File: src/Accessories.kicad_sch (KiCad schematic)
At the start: 20 parts

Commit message: Update Schematics design
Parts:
- removed D?: LED_Dual_Red_Green, LED_THT:LED_D5.0mm-3, symbol Device:LED_Dual_AAK
- removed R? (x2): 200R, Resistor_THT:R_Axial_DIN0204_L3.6mm_D1.6mm_P5.08mm_Horizontal, symbol Device:R
- added D? (x2): LED Yellow, LED_THT:LED_D5.0mm, symbol Device:LED
- added R? (x2): 470R, Resistor_THT:R_Axial_DIN0204_L3.6mm_D1.6mm_P5.08mm_Horizontal, symbol Device:R
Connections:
- net LowBat: now also R?.2
- net GND1 renamed GNDDash
- net GNDDash: now also D?.1 (K), D?.1 (K)
- net HighBat renamed PLight
- net PLight: now also R?.2
- new net: D?.2 (A), R?.1 (x2)
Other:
- note added: "Low battery indicator"
- note removed: "Battery indicator"
- moved on the sheet: D?, R?

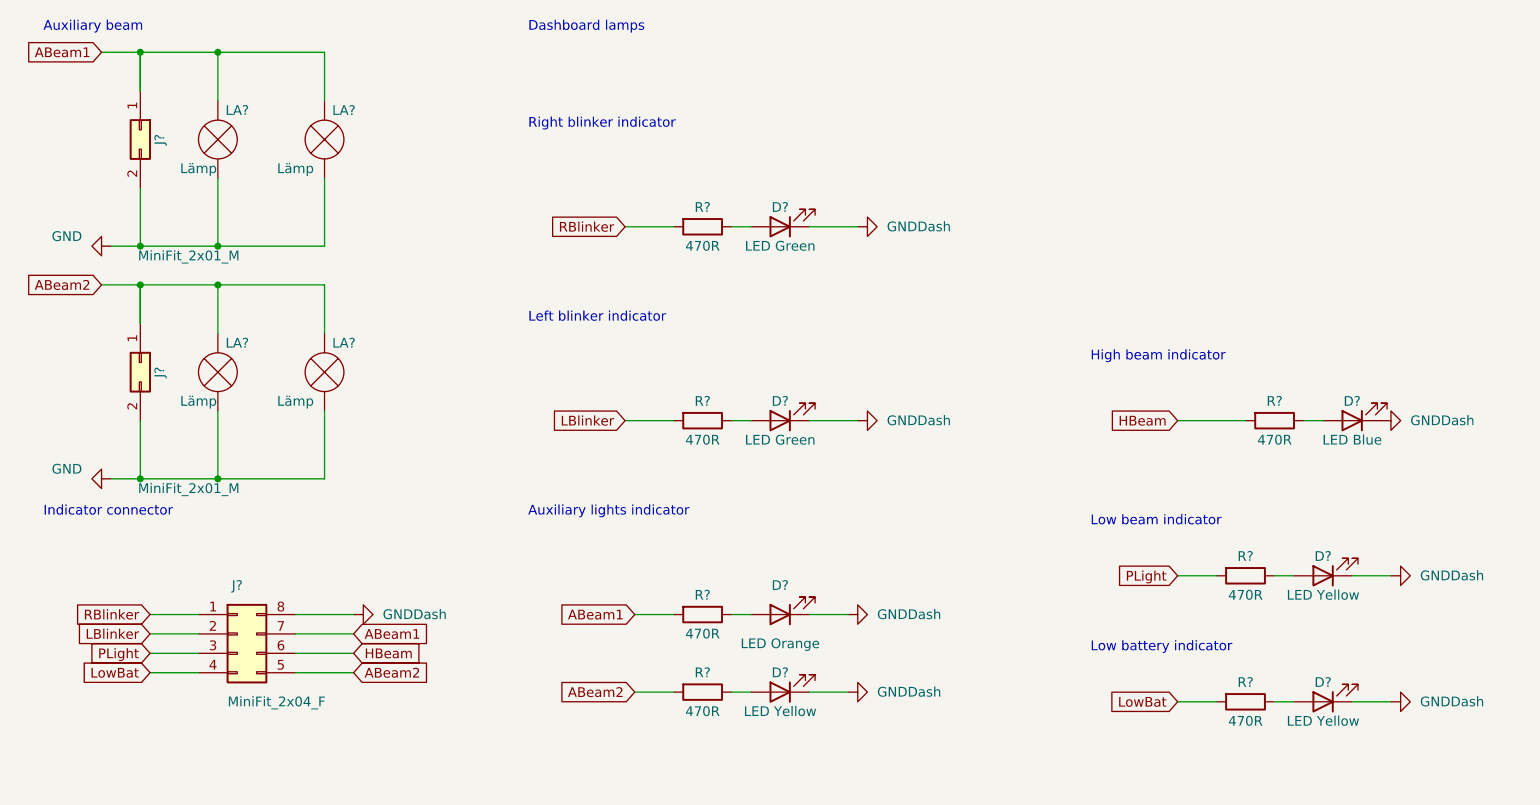
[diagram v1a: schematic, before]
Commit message: Add radio backup battery circuit; Update cable harness; rework main board circuit
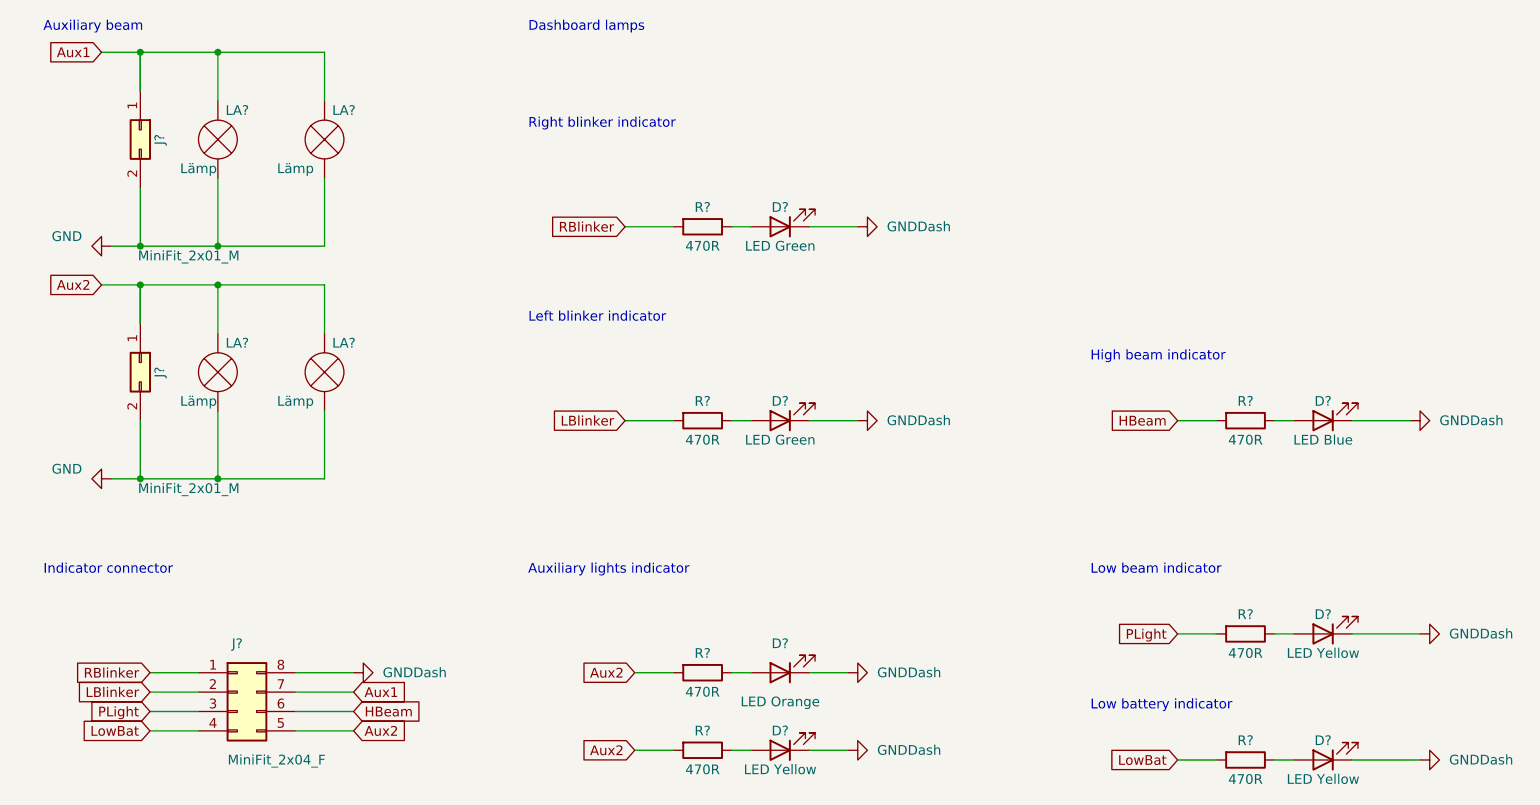
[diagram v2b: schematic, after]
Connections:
- net ABeam1 renamed Aux1
- net Aux1: no longer R?.2
- net ABeam2 renamed Aux2
- net Aux2: now also R?.2
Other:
- moved on the sheet: D?, J?, R?

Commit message: update Schematics
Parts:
- removed D? (x3): LED Yellow, LED_THT:LED_D5.0mm, symbol Device:LED
- removed J?: MiniFit_2x04_F, Connector_Molex:Molex_Mini-Fit_Jr_5566-08A_2x04_P4.20mm_Vertical, symbol Connector_Generic:Conn_02x04_Counter_Clockwise
- removed R? (x3): 470R, Resistor_THT:R_Axial_DIN0204_L3.6mm_D1.6mm_P5.08mm_Horizontal, symbol Device:R
- added D?: LED Green, LED_THT:LED_D5.0mm, symbol Device:LED
- added J?: MiniFit_2x03_F, Connector_Molex:Molex_Mini-Fit_Jr_5566-06A_2x03_P4.20mm_Vertical, symbol Connector_Generic:Conn_02x03_Counter_Clockwise
- added R?: 470R, Resistor_THT:R_Axial_DIN0204_L3.6mm_D1.6mm_P5.08mm_Horizontal, symbol Device:R
- D?: value LED Green -> LED Red
- D?: value LED Orange -> LED Yellow
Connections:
- net GNDDash: now also D?.1 (K), J?.6 (Pin_6)
- net HBeam: now also J?.5 (Pin_5)
- net LBlinker: now also J?.2 (Pin_2)
- net LowBat: now also R?.2, J?.3 (Pin_3)
- net RBlinker: now also J?.1 (Pin_1), R?.2; no longer R?.2
- net Aux1 renamed AuxHBeam
- net Aux2 renamed AuxLBeam
- net AuxLBeam: no longer R?.2
- new net: D?.2 (A), R?.1
- new net AuxBeams: J?.4 (Pin_4), R?.2
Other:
- note added: "Auxiliary beams"
- note added: "Auxiliary lights indicators"
- note added: "High beams"
- note added: "Indicators connector"
- note added: "Left signal indicator"
- note added: "Low battery Indicator"
- note added: "Medium beams"
- note added: "Right signal indicator"
- note removed: "Auxiliary beam"
- note removed: "Auxiliary lights indicator"
- note removed: "Indicator connector"
- note removed: "Left blinker indicator"
- note removed: "Low battery indicator"
- note removed: "Low beam indicator"
- note removed: "Right blinker indicator"
- moved on the sheet: D?, J?, LA?, R?

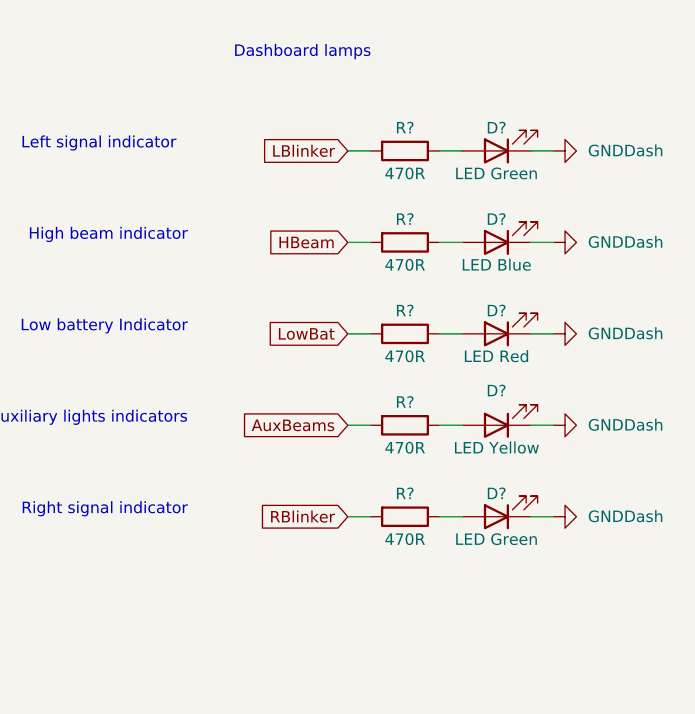
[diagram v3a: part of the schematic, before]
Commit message: Update Schmatics; Cleanup unecessary circuits; Simplify blinkers dimmers; Update PCB; Colorize motorcycle electric diagram.
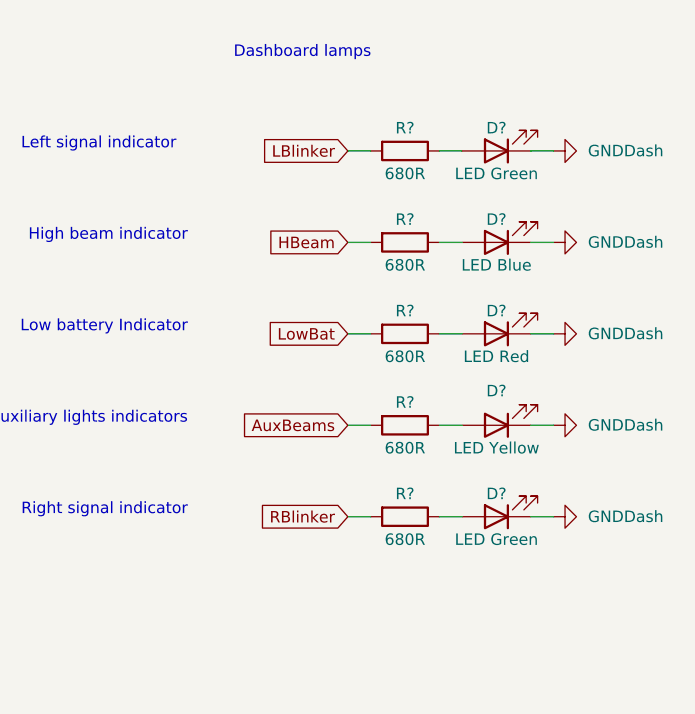
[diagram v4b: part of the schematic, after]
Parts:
- R? (x5): value 470R -> 680R

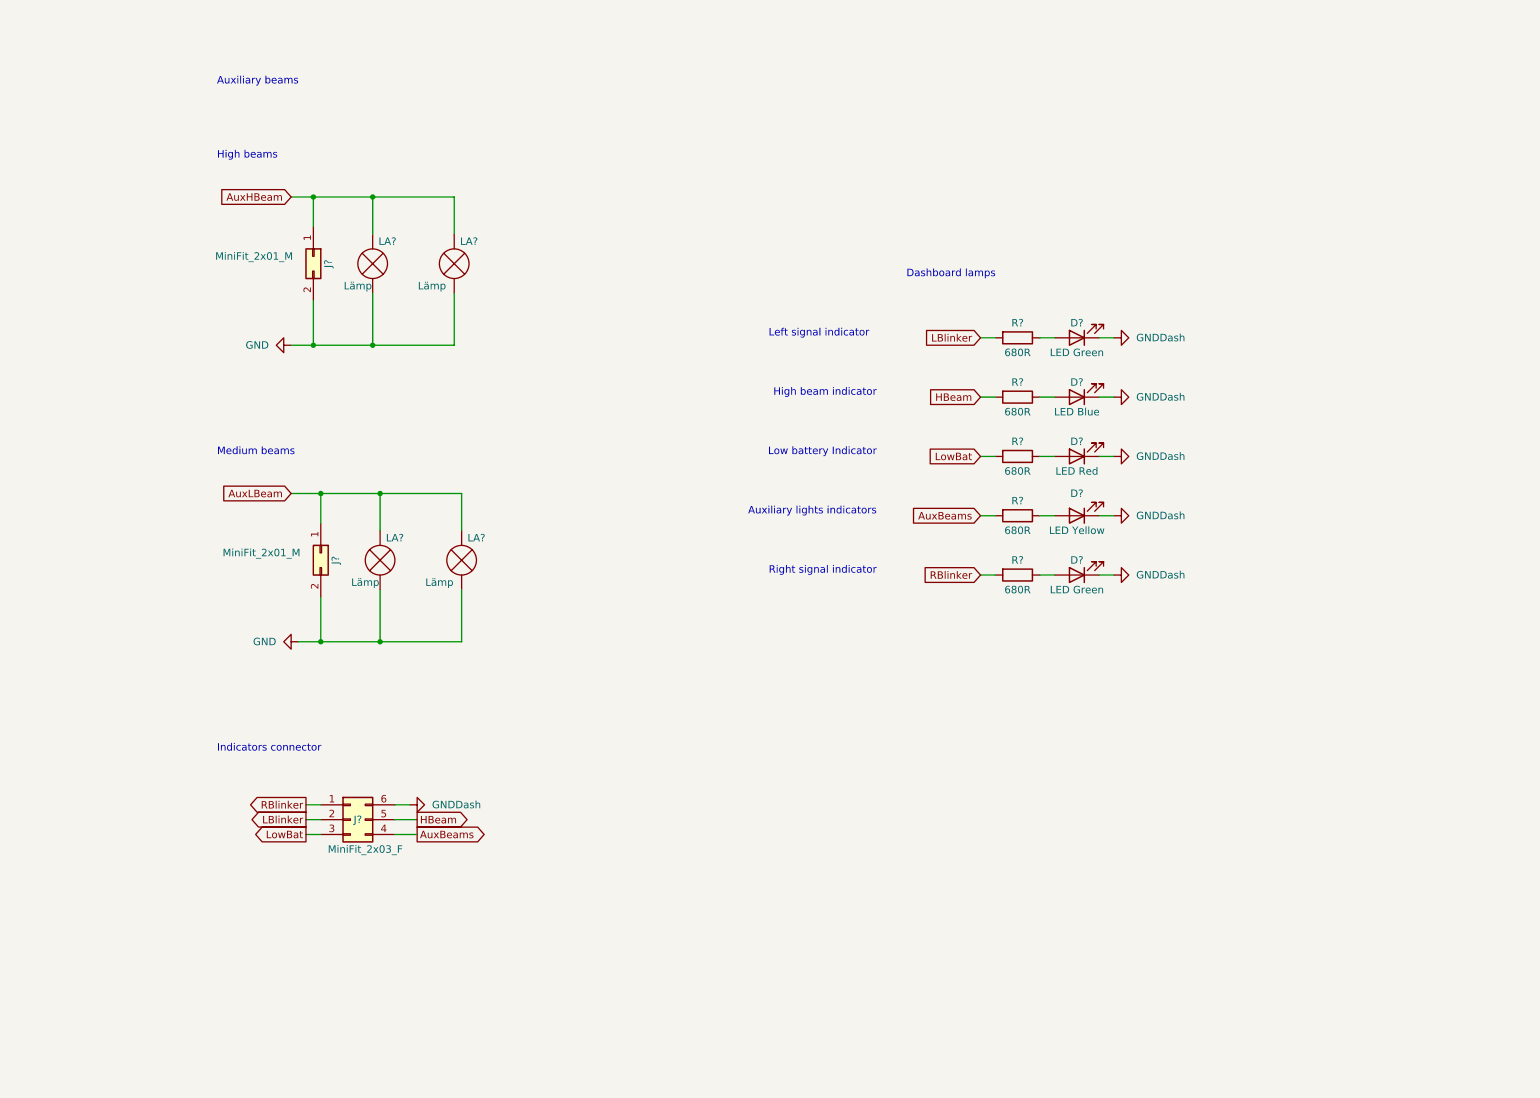
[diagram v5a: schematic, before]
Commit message: simplify circuit diagram. Remove unecessary features; Split board into two components|
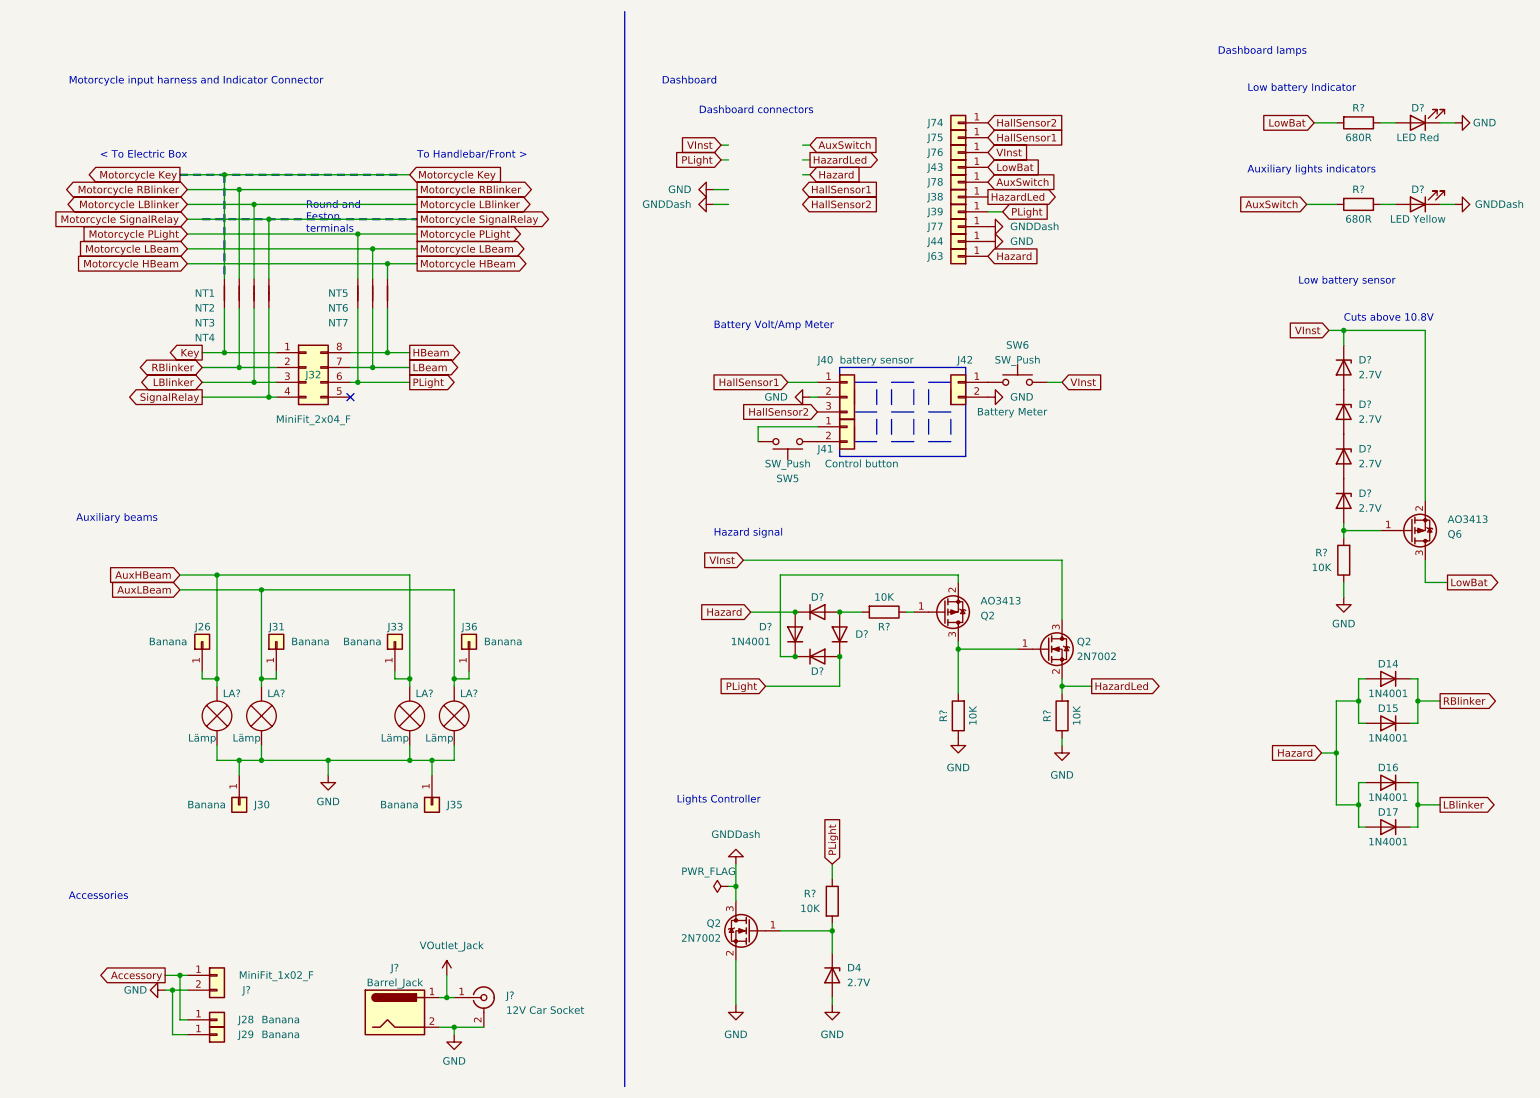
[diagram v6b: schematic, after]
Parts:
- removed D? (x2): LED Green, LED_THT:LED_D5.0mm, symbol Device:LED
- removed D?: LED Yellow, LED_THT:LED_D5.0mm, symbol Device:LED
- removed J?: MiniFit_2x03_F, Connector_Molex:Molex_Mini-Fit_Jr_5566-06A_2x03_P4.20mm_Vertical, symbol Connector_Generic:Conn_02x03_Counter_Clockwise
- removed J? (x2): MiniFit_2x01_M, Connector_Molex:Molex_Mini-Fit_Jr_5566-02A_2x01_P4.20mm_Vertical, symbol Connector_Generic:Conn_02x01
- removed LA? (x3): Lämp, symbol Device:Lamp
- removed R? (x3): 680R, Resistor_THT:R_Axial_DIN0204_L3.6mm_D1.6mm_P5.08mm_Horizontal, symbol Device:R
- added D14, D15, D16, D17, D? (x4): 1N4001, Diode_THT:D_DO-41_SOD81_P10.16mm_Horizontal, symbol Diode:1N4001
- added D4, D? (x4): 2.7V, Diode_THT:D_DO-35_SOD27_P7.62mm_Horizontal, symbol Diode:BZV55C2V7
- added J26, J28, J29, J30, J31, J33, J35, J36: Banana, symbol Connector_Generic:Conn_01x01
- added J32: MiniFit_2x04_F, symbol Connector_Generic:Conn_02x04_Counter_Clockwise
- added J38, J39, J43, J44, J63, J74, J75, J76, J77, J78: Conn_01x01, TestPoint:TestPoint_THTPad_D2.5mm_Drill1.2mm, symbol Connector_Generic:Conn_01x01
- added J40: battery sensor, symbol Connector_Generic:Conn_01x03
- added J41: Control button, symbol Connector_Generic:Conn_01x02
- added J42: Battery Meter, symbol Connector_Generic:Conn_01x02
- added J?: Barrel_Jack, symbol Connector:Barrel_Jack
- added J?: 12V Car Socket, symbol Connector:Conn_Coaxial
- added J?: MiniFit_1x02_F, symbol Connector_Generic:Conn_01x02
- added LA? (x3): Lämp, symbol Device:Lamp
- added NT1, NT2, NT3, NT4, NT5, NT6, NT7: NetTie_2, symbol Device:NetTie_2
- added Q2, Q6: AO3413, Package_TO_SOT_SMD:SOT-23, symbol Transistor_FET:AO3401A
- added Q2 (x2): 2N7002, Package_TO_SOT_SMD:SOT-23, symbol Transistor_FET:2N7002
- added R? (x5): 10K, Resistor_SMD:R_1206_3216Metric_Pad1.30x1.75mm_HandSolder, symbol Device:R
- added SW5, SW6: SW_Push, symbol Switch:SW_Push
- D?: value LED Blue -> LED Yellow
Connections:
- net AuxHBeam: now also J26.1 (Pin_1), J33.1 (Pin_1), LA?.1 (-), LA?.1 (-); no longer LA?.1 (-)
- net AuxLBeam: now also LA?.1 (-), J31.1 (Pin_1), J36.1 (Pin_1), LA?.1 (-)
- net GND: now also D?.1 (K), D4.2 (A), J29.1 (Pin_1), J30.1 (Pin_1), J35.1 (Pin_1), J40.2 (Pin_2), J42.2 (Pin_2), J44.1 (Pin_1), J?.2, J?.2 (Ext), J?.2 (Pin_2), LA?.2 (+), LA?.2 (+), LA?.2 (+), Q2.2 (S), R?.1, R?.1, R?.1
- net GNDDash: now also J77.1 (Pin_1), Q2.3 (D); no longer D?.1 (K)
- net HBeam: now also J32.8 (Pin_8), NT7.1; no longer R?.2
- net LBlinker: now also D16.1 (K), D17.1 (K), J32.3 (Pin_3), NT3.1
- net LowBat: now also J43.1 (Pin_1), Q6.3 (D)
- net RBlinker: now also D14.1 (K), D15.1 (K), J32.2 (Pin_2), NT2.1
- new net: Q2.1 (G), R?.1
- new net: D?.2 (A), D?.2 (A), R?.2
- new net: D4.1 (K), Q2.1 (G), R?.2
- new net: D?.2 (A), Q6.1 (G), R?.2
- new net: D?.1 (K), D?.2 (A) (x3)
- new net: Q2.1 (G), Q2.3 (D), R?.2
- new net: D?.1 (K), D?.1 (K), Q2.2 (S)
- new net: J41.1 (Pin_1), SW5.1
- new net: J41.2 (Pin_2), SW5.2
- new net: J42.1 (Pin_1), SW6.2
- new net Accessory: J28.1 (Pin_1), J?.1 (Pin_1)
- new net AuxSwitch: J78.1 (Pin_1), R?.2
- new net HallSensor1: J40.1 (Pin_1), J75.1 (Pin_1)
- new net HallSensor2: J40.3 (Pin_3), J74.1 (Pin_1)
- new net Hazard: D14.2 (A), D15.2 (A), D16.2 (A), D17.2 (A), D?.1 (K), D?.2 (A), J63.1 (Pin_1)
- new net HazardLed: J38.1 (Pin_1), Q2.2 (S), R?.2
- new net Key: J32.1 (Pin_1), NT1.1
- new net LBeam: J32.7 (Pin_7), NT6.1
- new net Motorcycle HBeam: NT7.2
- new net Motorcycle Key: NT1.2
- new net Motorcycle LBeam: NT6.2
- new net Motorcycle LBlinker: NT3.2
- new net Motorcycle PLight: NT5.2
- new net Motorcycle RBlinker: NT2.2
- new net Motorcycle SignalRelay: NT4.2
- new net PLight: D?.1 (K), D?.2 (A), J32.6 (Pin_6), J39.1 (Pin_1), NT5.1, R?.1
- new net SignalRelay: J32.4 (Pin_4), NT4.1
- new net VInst: D?.1 (K), J76.1 (Pin_1), Q2.3 (D), Q6.2 (S), SW6.1
- new net VOutlet_Jack: J?.1, J?.1 (In)
- no-connect marks 0 -> 1
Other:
- note added: "< To Electric Box"
- note added: "Accessories"
- note added: "Battery Volt/Amp Meter"
- note added: "Cuts above 10.8V"
- note added: "Dashboard"
- note added: "Dashboard connectors"
- note added: "Hazard signal"
- note added: "Lights Controller"
- note added: "Low battery sensor"
- note added: "Motorcycle input harness and Indicator Connector"
- note added: "Round and Feston terminals"
- note added: "To Handlebar/Front >"
- note removed: "High beam indicator"
- note removed: "High beams"
- note removed: "Indicators connector"
- note removed: "Left signal indicator"
- note removed: "Medium beams"
- note removed: "Right signal indicator"
- moved on the sheet: D?, LA?, R?
